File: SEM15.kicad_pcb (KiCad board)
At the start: 2 copper layers, 213.5 x 50.2 mm, 24 parts

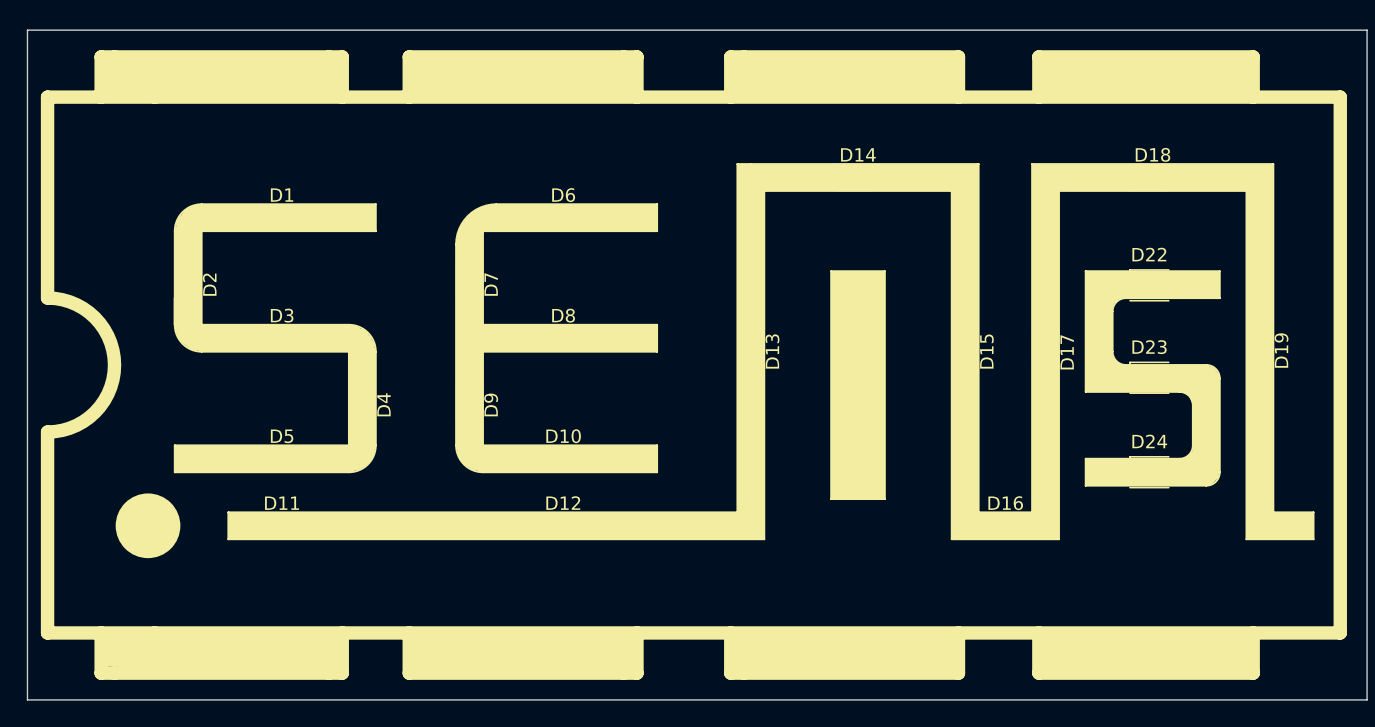
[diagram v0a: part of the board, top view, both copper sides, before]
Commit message: rgb es feher led meghajtasa, mikrovezerlo, pcb-n alkatreszrendezgets
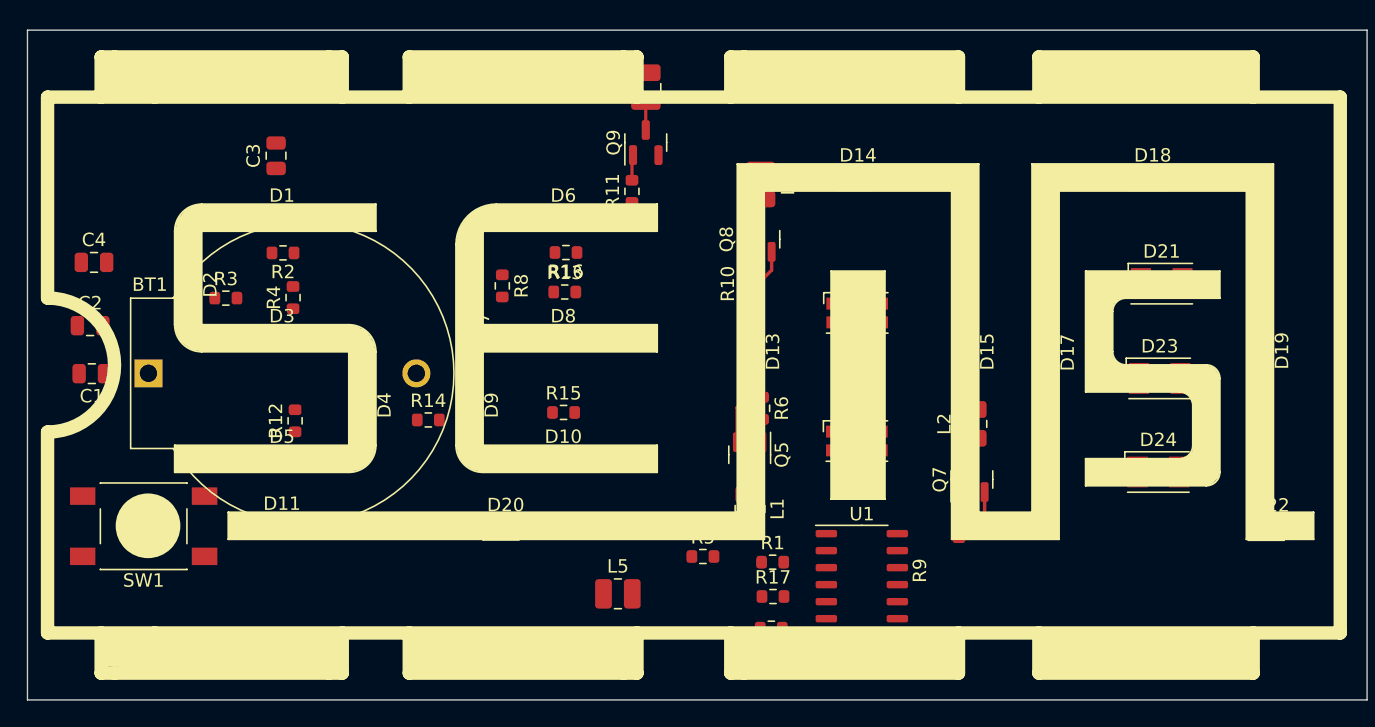
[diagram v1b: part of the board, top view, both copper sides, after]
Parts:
- added BT1: Battery, karifa:CR2032_Holder, F.Cu at (31.0, 50.6)
- added C1: C, Capacitor_SMD:C_0805_2012Metric, F.Cu at (26.8, 50.6)
- added C2: C, Capacitor_SMD:C_0805_2012Metric, F.Cu at (26.7, 47.1)
- added C3: C, Capacitor_SMD:C_0805_2012Metric, F.Cu at (40.6, 34.4)
- added C4: C, Capacitor_SMD:C_0805_2012Metric, F.Cu at (27.0, 42.3)
- added L1: L, Inductor_SMD:L_1008_2520Metric, F.Cu at (75.9, 60.7)
- added L2: L, Inductor_SMD:L_1008_2520Metric, F.Cu at (92.5, 54.4)
- added L3: L, Inductor_SMD:L_1008_2520Metric, F.Cu at (76.7, 36.5)
- added L4: L, Inductor_SMD:L_1008_2520Metric, F.Cu at (68.2, 29.2)
- added L5: L, Inductor_SMD:L_1008_2520Metric, F.Cu at (66.1, 67.1)
- added Q5: AO3401A, sajat:SOT-23, F.Cu at (75.9, 56.7)
- added Q7: AO3401A, sajat:SOT-23, F.Cu at (92.5, 58.5)
- added Q8: AO3401A, sajat:SOT-23, F.Cu at (76.6, 40.6)
- added Q9: AO3401A, sajat:SOT-23, F.Cu at (68.2, 33.4)
- added R1: R, Resistor_SMD:R_0603_1608Metric, F.Cu at (77.6, 64.7)
- added R10: 100k, Resistor_SMD:R_0603_1608Metric, F.Cu at (75.7, 43.9)
- added R11: 100k, Resistor_SMD:R_0603_1608Metric, F.Cu at (67.1, 37.0)
- added R12: R, Resistor_SMD:R_0603_1608Metric, F.Cu at (42.0, 54.2)
- added R13: R, Resistor_SMD:R_0603_1608Metric, F.Cu at (62.1, 44.5)
- added R14: R, Resistor_SMD:R_0603_1608Metric, F.Cu at (51.9, 54.1)
- added R15: R, Resistor_SMD:R_0603_1608Metric, F.Cu at (62.0, 53.5)
- added R16: R, Resistor_SMD:R_0603_1608Metric, F.Cu at (62.2, 41.6)
- added R17: R, Resistor_SMD:R_0603_1608Metric, F.Cu at (77.7, 67.3)
- added R2: R, Resistor_SMD:R_0603_1608Metric, F.Cu at (41.1, 41.6)
- added R3: R, Resistor_SMD:R_0603_1608Metric, F.Cu at (36.8, 45.0)
- added R4: R, Resistor_SMD:R_0603_1608Metric, F.Cu at (41.8, 45.0)
- added R5: R, Resistor_SMD:R_0603_1608Metric, F.Cu at (72.4, 64.3)
- added R6: 100k, Resistor_SMD:R_0603_1608Metric, F.Cu at (76.9, 53.2)
- added R7: R, Resistor_SMD:R_0603_1608Metric, F.Cu at (77.5, 69.6)
- added R8: R, Resistor_SMD:R_0603_1608Metric, F.Cu at (57.4, 44.1)
- added R9: 100k, Resistor_SMD:R_0603_1608Metric, F.Cu at (91.5, 62.1)
- added SW1: SW_DPST_x2, sajat:SW_Push_K2-1102SP, F.Cu at (30.7, 62.0)
- added U1: STC8G1K08-SOP16, Package_SO:STC_SOP-16_3.9x9.9mm_P1.27mm, F.Cu at (84.3, 67.0)
- D12, D16: value LED -> LED_ARGB; footprint LED_SMD:LED_0805_2012Metric -> LED_SMD:LED_RGB_Wuerth-PLCC4_3.2x2.8mm_150141M173100
- D20, D22: value LED_KGRB -> LED; footprint LED_SMD:LED_Cree-PLCC4_2x2mm_CW -> LED_SMD:LED_0805_2012Metric
- D21, D23, D24: value LED_KGRB -> LED_ARGB; footprint LED_SMD:LED_Cree-PLCC4_2x2mm_CW -> LED_SMD:LED_RGB_Wuerth-PLCC4_3.2x2.8mm_150141M173100
- moved D20 31.0 mm to (57.7, 62.1)
- moved D12 27.1 mm to (83.9, 46.1)
- moved D21 26.2 mm to (106.7, 43.9)
- moved D22 20.2 mm to (114.8, 62.1)
- moved D16 12.8 mm to (83.9, 55.7)
- moved D23 0.77 mm to (106.5, 51.0)
- moved D24 0.67 mm to (106.4, 58.0)
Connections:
- D1 pad 1: unconnected-(D1-K-Pad1) -> Net-(D1-K)
- D1 pad 2: unconnected-(D1-A-Pad2) -> Net-(D1-A)
- D10 pad 1: unconnected-(D10-K-Pad1) -> Net-(D10-K)
- D10 pad 2: unconnected-(D10-A-Pad2) -> Net-(D10-A)
- D11 pad 1: unconnected-(D11-K-Pad1) -> Net-(D11-K)
- D11 pad 2: unconnected-(D11-A-Pad2) -> Earth
- D12 pad 1: unconnected-(D12-K-Pad1) -> GND
- D12 pad 2: unconnected-(D12-A-Pad2) -> /LED_VCC_15_B
- D13 pad 1: unconnected-(D13-K-Pad1) -> Net-(D11-K)
- D13 pad 2: unconnected-(D13-A-Pad2) -> Earth
- D14 pad 1: unconnected-(D14-K-Pad1) -> Net-(D11-K)
- D14 pad 2: unconnected-(D14-A-Pad2) -> Earth
- D15 pad 1: unconnected-(D15-K-Pad1) -> Net-(D11-K)
- D15 pad 2: unconnected-(D15-A-Pad2) -> Earth
- D16 pad 1: unconnected-(D16-K-Pad1) -> GND
- D16 pad 2: unconnected-(D16-A-Pad2) -> /LED_VCC_15_B
- D17 pad 1: unconnected-(D17-K-Pad1) -> Net-(D11-K)
- D17 pad 2: unconnected-(D17-A-Pad2) -> Earth
- D18 pad 1: unconnected-(D18-K-Pad1) -> Net-(D11-K)
- D18 pad 2: unconnected-(D18-A-Pad2) -> Earth
- D19 pad 1: unconnected-(D19-K-Pad1) -> Net-(D11-K)
- D19 pad 2: unconnected-(D19-A-Pad2) -> Earth
- D2 pad 1: unconnected-(D2-K-Pad1) -> Net-(D1-K)
- D2 pad 2: unconnected-(D2-A-Pad2) -> Net-(D2-A)
- D20 pad 1: unconnected-(D20-K-Pad1) -> Net-(D11-K)
- D20 pad 2: unconnected-(D20-GA-Pad2) -> Earth
- D21 pad 1: unconnected-(D21-K-Pad1) -> GND
- D22 pad 1: unconnected-(D22-K-Pad1) -> Net-(D11-K)
- D22 pad 2: unconnected-(D22-GA-Pad2) -> Earth
- D23 pad 1: unconnected-(D23-K-Pad1) -> GND
- D23 pad 2: unconnected-(D23-GA-Pad2) -> /LED_VCC_15_B
- D23 pad 3: unconnected-(D23-RA-Pad3) -> /LED_VCC_15_G
- D23 pad 4: unconnected-(D23-BA-Pad4) -> /LED_VCC_15_R
- D24 pad 1: unconnected-(D24-K-Pad1) -> GND
- D24 pad 2: unconnected-(D24-GA-Pad2) -> /LED_VCC_15_B
- D24 pad 3: unconnected-(D24-RA-Pad3) -> /LED_VCC_15_G
- D24 pad 4: unconnected-(D24-BA-Pad4) -> /LED_VCC_15_R
- D3 pad 1: unconnected-(D3-K-Pad1) -> Net-(D1-K)
- D3 pad 2: unconnected-(D3-A-Pad2) -> Net-(D3-A)
- D4 pad 1: unconnected-(D4-K-Pad1) -> Net-(D1-K)
- D4 pad 2: unconnected-(D4-A-Pad2) -> Net-(D4-A)
- D5 pad 1: unconnected-(D5-K-Pad1) -> Net-(D1-K)
- D5 pad 2: unconnected-(D5-A-Pad2) -> Net-(D5-A)
- D6 pad 1: unconnected-(D6-K-Pad1) -> Net-(D10-K)
- D6 pad 2: unconnected-(D6-A-Pad2) -> Net-(D6-A)
- D7 pad 1: unconnected-(D7-K-Pad1) -> Net-(D10-K)
- D7 pad 2: unconnected-(D7-A-Pad2) -> Net-(D7-A)
- D8 pad 1: unconnected-(D8-K-Pad1) -> Net-(D10-K)
- D8 pad 2: unconnected-(D8-A-Pad2) -> Net-(D8-A)
- D9 pad 1: unconnected-(D9-K-Pad1) -> Net-(D10-K)
- D9 pad 2: unconnected-(D9-A-Pad2) -> Net-(D9-A)
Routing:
- net VCC: track 0.00 -> 13.0 mm
- net Net-(Q5-D): track 0.00 -> 2.30 mm
- net Net-(Q7-D): track 0.00 -> 2.14 mm
- net Net-(Q9-D): track 0.00 -> 2.13 mm
- net Net-(D11-K): track 0.00 -> 1.91 mm
- net /LED_VCC_15_G: track 0.00 -> 1.76 mm
- net /LED_VCC_15_R: track 0.00 -> 1.71 mm
- net /LED_VCC_15_B: track 0.00 -> 1.59 mm

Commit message: sch kesz
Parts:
- removed R12, R13, R14, R15, R16, R2, R3, R4, R8: R, Resistor_SMD:R_0603_1608Metric
- added D25: LED, LED_SMD:LED_0805_2012Metric, F.Cu at (76.1, 88.1)
- added D26: LED, LED_SMD:LED_0805_2012Metric, F.Cu at (76.1, 91.1)
- added D27: LED, LED_SMD:LED_0805_2012Metric, F.Cu at (76.1, 94.1)
- added D28: LED, LED_SMD:LED_0805_2012Metric, F.Cu at (76.1, 97.2)
- added D29: LED, LED_SMD:LED_0805_2012Metric, F.Cu at (76.1, 100.2)
- added J1: Conn_01x04, Connector_PinHeader_1.27mm:PinHeader_1x04_P1.27mm_Vertical, F.Cu at (85.3, 88.2)
- added Q1: AO3401A, sajat:SOT-23, F.Cu at (51.0, 62.5)
- added Q2: AO3401A, sajat:SOT-23, F.Cu at (51.0, 67.0)
- added Q3: AO3401A, sajat:SOT-23, F.Cu at (80.8, 88.8)
- added Q4: AO3401A, sajat:SOT-23, F.Cu at (80.8, 93.2)
- D12, D16, D21: value LED_ARGB -> LED; footprint LED_SMD:LED_RGB_Wuerth-PLCC4_3.2x2.8mm_150141M173100 -> LED_SMD:LED_0805_2012Metric
- R1: value R -> 100k
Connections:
- D1 pad 2: Net-(D1-A) -> Earth
- D10 pad 2: Net-(D10-A) -> Earth
- D11 pad 1: Net-(D11-K) -> /LED_EN_M1
- D11 pad 2: Earth -> Net-(D11-A)
- D12 pad 1: GND -> Net-(D12-K)
- D12 pad 2: /LED_VCC_15_B -> Net-(D12-A)
- D13 pad 1: Net-(D11-K) -> /LED_EN_M1
- D13 pad 2: Earth -> Net-(D11-A)
- D14 pad 1: Net-(D11-K) -> /LED_EN_M2
- D14 pad 2: Earth -> Net-(D14-A)
- D15 pad 1: Net-(D11-K) -> /LED_EN_M3
- D15 pad 2: Earth -> Net-(D15-A)
- D16 pad 1: GND -> Net-(D12-K)
- D16 pad 2: /LED_VCC_15_B -> Net-(D12-A)
- D17 pad 1: Net-(D11-K) -> /LED_EN_M4
- D17 pad 2: Earth -> Net-(D17-A)
- D18 pad 1: Net-(D11-K) -> /LED_EN_M5
- D18 pad 2: Earth -> Net-(D18-A)
- D19 pad 1: Net-(D11-K) -> /LED_EN_M6
- D19 pad 2: Earth -> Net-(D19-A)
- D2 pad 2: Net-(D2-A) -> Earth
- D20 pad 1: Net-(D11-K) -> /LED_EN_M7
- D20 pad 2: Earth -> Net-(D20-A)
- D21 pad 1: GND -> Net-(D12-K)
- D21 pad 2: unconnected-(D21-RK-Pad2) -> Net-(D12-A)
- D22 pad 1: Net-(D11-K) -> /LED_EN_M7
- D22 pad 2: Earth -> Net-(D20-A)
- D23 pad 2: /LED_VCC_15_B -> Net-(D12-RK)
- D23 pad 3: /LED_VCC_15_G -> Net-(D12-GK)
- D23 pad 4: /LED_VCC_15_R -> Net-(D23-BK)
- D24 pad 2: /LED_VCC_15_B -> Net-(D12-RK)
- D24 pad 3: /LED_VCC_15_G -> Net-(D12-GK)
- D24 pad 4: /LED_VCC_15_R -> Net-(D23-BK)
- D3 pad 2: Net-(D3-A) -> Earth
- D4 pad 2: Net-(D4-A) -> Earth
- D5 pad 2: Net-(D5-A) -> Earth
- D6 pad 2: Net-(D6-A) -> Earth
- D7 pad 2: Net-(D7-A) -> Earth
- D8 pad 2: Net-(D8-A) -> Earth
- D9 pad 2: Net-(D9-A) -> Earth
- L1 pad 1: Net-(Q5-D) -> Net-(D12-K)
- L2 pad 1: Net-(Q7-D) -> Net-(D25-K)
- L3 pad 1: Net-(Q8-D) -> Net-(D12-RK)
- L4 pad 1: Net-(Q9-D) -> Net-(D1-K)
- Q5 pad 3: Net-(Q5-D) -> Net-(D12-BK)
- Q7 pad 3: Net-(Q7-D) -> Net-(D12-GK)
- Q8 pad 3: Net-(Q8-D) -> Net-(D12-RK)
- R1 pad 1: /LED_EN_S -> VCC
- R1 pad 2: Net-(Q1-G) -> /LED_EN_E
- R11 pad 2: Net-(D11-K) -> /LED_EN_S
- R6 pad 2: /LED_VCC_15_R -> /LED_EN_1
- R9 pad 2: /LED_VCC_15_G -> /LED_EN_5
- U1 pad 10: unconnected-(U1-P3.1-Pad10) -> /P3.1
- U1 pad 12: unconnected-(U1-P3.3-Pad12) -> /LED_EN_M5
- U1 pad 13: unconnected-(U1-P3.4-Pad13) -> /LED_EN_M6
- U1 pad 14: unconnected-(U1-P3.5-Pad14) -> /LED_EN_M7
- U1 pad 15: unconnected-(U1-P3.6-Pad15) -> /LED_EN_1
- U1 pad 16: unconnected-(U1-P3.7-Pad16) -> /LED_EN_5
- U1 pad 3: /LED_EN_M -> /LED_EN_M1
- U1 pad 4: /LED_VCC_15_R -> /LED_EN_M2
- U1 pad 5: /LED_VCC_15_G -> /LED_EN_M3
- U1 pad 7: /LED_VCC_15_B -> /LED_EN_M4
- U1 pad 9: unconnected-(U1-P3.0-Pad9) -> /P3.0
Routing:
- net Net-(Q5-D): track 2.30 -> 0.00 mm
- net Net-(D12-BK): track 0.00 -> 2.30 mm
- net Net-(Q7-D): track 2.14 -> 0.00 mm
- net Net-(D12-GK): track 0.00 -> 2.14 mm

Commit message: pcb nagyreszt
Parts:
- removed C1, C2: C, Capacitor_SMD:C_0805_2012Metric
- removed D16: LED, LED_SMD:LED_0805_2012Metric
- removed L3: L, Inductor_SMD:L_1008_2520Metric
- removed Q5, Q7, Q8, Q9: AO3401A, sajat:SOT-23
- removed R10: 100k, Resistor_SMD:R_0603_1608Metric
- removed R17: R, Resistor_SMD:R_0603_1608Metric
- added R12: R, Resistor_SMD:R_0603_1608Metric, F.Cu at (115.4, 65.6)
- added R2: 510, Resistor_SMD:R_0603_1608Metric, F.Cu at (54.6, 63.8)
- added R3: 1k, Resistor_SMD:R_0603_1608Metric, F.Cu at (72.4, 59.6)
- added R4: 510, Resistor_SMD:R_0603_1608Metric, F.Cu at (88.9, 39.1)
- added R8: R, Resistor_SMD:R_0603_1608Metric, F.Cu at (78.8, 44.6)
- D23, D24: value LED_ARGB -> LED; footprint LED_SMD:LED_RGB_Wuerth-PLCC4_3.2x2.8mm_150141M173100 -> LED_SMD:LED_0805_2012Metric
- moved D20 58.2 mm to (114.1, 47.5), turned to 90 degrees
- moved D28 54.6 mm to (110.0, 54.4), turned to 90 degrees
- moved D25 53.3 mm to (106.0, 44.0)
- moved D27 52.7 mm to (106.4, 51.1)
- moved D29 51.6 mm to (106.0, 58.2)
- moved D26 50.5 mm to (102.1, 47.8), turned to 90 degrees
- moved L4 43.6 mm to (47.5, 67.6), turned to 180 degrees
- moved R7 39.6 mm to (101.6, 38.2)
- moved Q4 38.9 mm to (109.4, 66.8), turned to -90 degrees
- moved Q3 35.3 mm to (88.7, 54.4), turned to -90 degrees
- moved R11 32.9 mm to (54.5, 67.4), turned to -90 degrees
- moved D23 30.7 mm to (76.0, 48.0), turned to 90 degrees
- moved D14 27.2 mm to (76.0, 62.0)
- moved J1 27.2 mm to (99.7, 65.2), turned to 90 degrees
- moved R5 23.5 mm to (95.3, 59.0), turned to 180 degrees
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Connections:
- BT1 pad 2: Earth -> GND
- C3 pad 2: Earth -> GND
- C4 pad 2: Earth -> GND
- D1 pad 2: Earth -> GND
- D10 pad 2: Earth -> GND
- D12 pad 2: Net-(D12-A) -> GND
- D15 pad 1: /LED_EN_M3 -> /LED_EN_M4
- D17 pad 1: /LED_EN_M4 -> /LED_EN_M5
- D18 pad 1: /LED_EN_M5 -> /LED_EN_M6
- D19 pad 2: Net-(D19-A) -> Net-(D18-A)
- D2 pad 2: Earth -> GND
- D21 pad 2: Net-(D12-A) -> GND
- D23 pad 1: GND -> /LED_EN_M3
- D23 pad 2: Net-(D12-RK) -> Net-(D23-A)
- D24 pad 1: GND -> /LED_EN_M4
- D24 pad 2: Net-(D12-RK) -> Net-(D15-A)
- D25 pad 2: Earth -> GND
- D26 pad 2: Earth -> GND
- D27 pad 2: Earth -> GND
- D28 pad 2: Earth -> GND
- D29 pad 2: Earth -> GND
- D3 pad 2: Earth -> GND
- D4 pad 2: Earth -> GND
- D5 pad 2: Earth -> GND
- D6 pad 2: Earth -> GND
- D7 pad 2: Earth -> GND
- D8 pad 2: Earth -> GND
- D9 pad 2: Earth -> GND
- L5 pad 1: Net-(Q2-D) -> Net-(D10-K)
- Q2 pad 3: Net-(Q2-D) -> Net-(D10-K)
- R5 pad 1: Net-(D4-A) -> Net-(D17-A)
- R7 pad 1: /LED_EN_E -> Net-(D18-A)
- R7 pad 2: Net-(Q6-G) -> VCC
- SW1 pad 1: Net-(SW1A-A) -> /SW_IN
- U1 pad 1: /LED_EN_S -> /LED_EN_M4
- U1 pad 11: Net-(SW1A-A) -> /LED_EN_M7
- U1 pad 12: /LED_EN_M5 -> /LED_EN_5
- U1 pad 14: /LED_EN_M7 -> /LED_EN_M5
- U1 pad 15: /LED_EN_1 -> /SW_IN
- U1 pad 16: /LED_EN_5 -> /LED_EN_1
- U1 pad 2: /LED_EN_E -> /LED_EN_M3
- U1 pad 3: /LED_EN_M1 -> /LED_EN_M2
- U1 pad 4: /LED_EN_M2 -> /LED_EN_M1
- U1 pad 5: /LED_EN_M3 -> /LED_EN_E
- U1 pad 7: /LED_EN_M4 -> /LED_EN_S
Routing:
- net VCC: track 13.0 -> 210.6 mm, vias 0 -> 6
- net /SW_IN: track 0.00 -> 71.6 mm, vias 0 -> 2
- net Net-(D1-K): track 0.00 -> 52.2 mm
- net /LED_EN_M7: track 0.00 -> 49.8 mm
- net /LED_EN_M1: track 0.00 -> 47.3 mm, vias 0 -> 2
- net Net-(D10-K): track 0.00 -> 43.4 mm
- net /LED_EN_M6: track 0.00 -> 43.1 mm
- net /LED_EN_M4: track 0.00 -> 42.5 mm
- net Net-(D25-K): track 0.00 -> 32.5 mm
- net /LED_EN_S: track 0.00 -> 30.0 mm
- net /LED_EN_5: track 0.00 -> 23.5 mm
- net Net-(D20-A): track 0.00 -> 20.7 mm
- net /LED_EN_E: track 0.00 -> 19.8 mm
- net Net-(D11-A): track 0.00 -> 19.7 mm
- net /LED_EN_M3: track 0.00 -> 18.8 mm
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- added copper zone on F.Cu, net GND
